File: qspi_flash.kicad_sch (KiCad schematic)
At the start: 5 parts, among them SW1 BOOTSEL, U2 W25Q128JVS

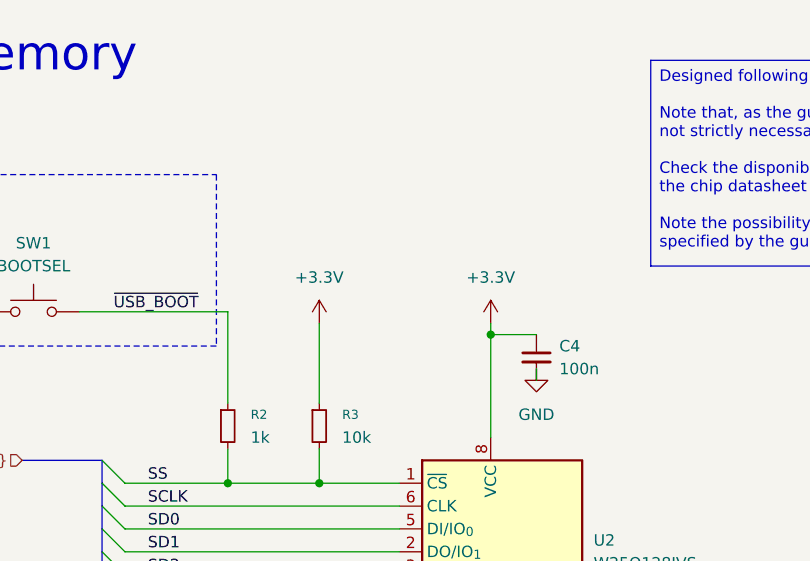
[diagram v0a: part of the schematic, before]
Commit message: NET allignment (all on +3V3)
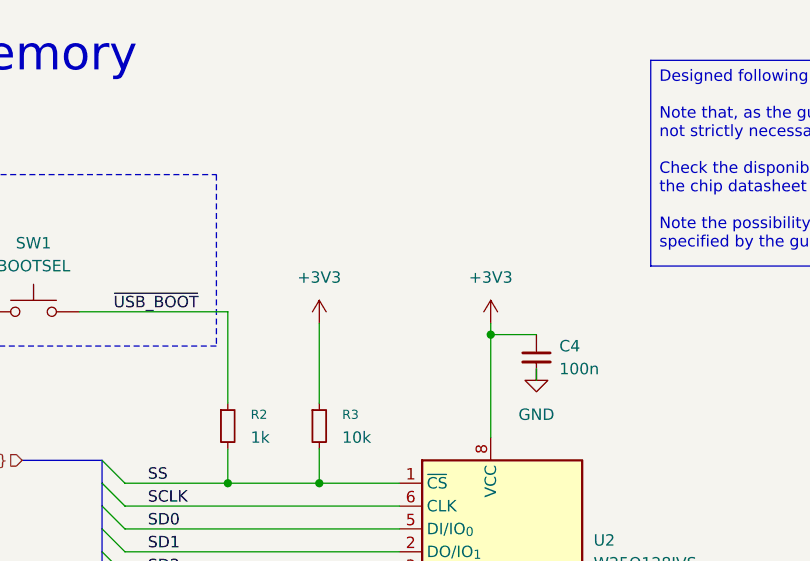
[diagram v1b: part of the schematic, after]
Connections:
- net +3.3V renamed +3V3
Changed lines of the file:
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@@
 			)
 		)
-		(property "Value" "+3.3V"
+		(property "Value" "+3V3"
 			(at 88.9 43.18 0)
 			(effects
@@
 			)
 		)
-		(property "Description" "Power symbol creates a global label with name \"+3.3V\""
+		(property "Description" "Power symbol creates a global label with name \"+3V3\""
 			(at 88.9 48.26 0)
 			(effects
@@
 			)
 		)
-		(property "Value" "+3.3V"
+		(property "Value" "+3V3"
 			(at 107.95 43.18 0)
 			(effects
@@
 			)
 		)
-		(property "Description" "Power symbol creates a global label with name \"+3.3V\""
+		(property "Description" "Power symbol creates a global label with name \"+3V3\""
 			(at 107.95 48.26 0)
 			(effects
